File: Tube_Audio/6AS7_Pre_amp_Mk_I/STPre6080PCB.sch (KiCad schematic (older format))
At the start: 50 parts, among them J101 Screw_Terminal_01x02, J102 Screw_Terminal_01x04, J103 Screw_Terminal_01x03, J203 Screw_Terminal_01x03, Q101 ZVN0545A, Q102 ZVN0545A, Q201 ZVN0545A, Q202 ZVN0545A

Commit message: Checkpoint -- getting closer to laying out the tone control PCB.
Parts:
- C101, C201: footprint (none) -> jrt-Capacitors:C_Rect_L13.0mm_W5.0mm_P7.50mm
- C102, C106, C202, C206: footprint (none) -> Capacitor_THT:C_Rect_L18.0mm_W8.0mm_P15.00mm_FKS3_FKP3
- C103, C203: footprint (none) -> jrt-Capacitors:C_Rect_L18.0mm_W9.0mm_P8.70mm
- C104, C105, C204, C205: footprint (none) -> jrt-Capacitors:C_Rect_L13.0mm_W6.0mm_P5.90mm
- J101: footprint (none) -> TerminalBlock:TerminalBlock_bornier-2_P5.08mm
- J102: footprint (none) -> TerminalBlock:TerminalBlock_bornier-4_P5.08mm
- J103, J203: footprint (none) -> TerminalBlock:TerminalBlock_bornier-3_P5.08mm
- Q101, Q102, Q201, Q202: footprint (none) -> Package_TO_SOT_THT:TO-92_HandSolder
- R101, R201: footprint (none) -> Resistor_THT:R_Axial_DIN0414_L11.9mm_D4.5mm_P15.24mm_Horizontal; Part (none) -> KOA Speer MF1/2DC4703F
- R102, R202, R203: footprint (none) -> Resistor_THT:R_Axial_DIN0414_L11.9mm_D4.5mm_P15.24mm_Horizontal; Part (none) -> Vishay HVR3700001005FR500
- R103: footprint (none) -> Resistor_THT:R_Axial_DIN0414_L11.9mm_D4.5mm_P15.24mm_Horizontal; Part (none) -> HVR3700001005FR500
- R104, R112, R204, R212: footprint (none) -> Resistor_THT:R_Axial_DIN0414_L11.9mm_D4.5mm_P15.24mm_Horizontal
- R105, R113, R205, R213: value 56K -> 47K; footprint (none) -> Resistor_THT:R_Axial_DIN0414_L11.9mm_D4.5mm_P15.24mm_Horizontal; Part (none) -> TE H4P47KFZA
- R106, R107, R108, R109, R206, R207, R208, R209: footprint (none) -> Resistor_THT:R_Axial_DIN0207_L6.3mm_D2.5mm_P10.16mm_Horizontal; Part (none) -> TE H856KBDA
- R110, R210: footprint (none) -> Resistor_THT:R_Axial_DIN0207_L6.3mm_D2.5mm_P10.16mm_Horizontal; Part (none) -> TE H8470KBZA
- R111, R211: value 220K -> 221K; footprint (none) -> Resistor_THT:R_Axial_DIN0207_L6.3mm_D2.5mm_P10.16mm_Horizontal; Part (none) -> TE YR1B221KCC
- RV101, RV102, RV201, RV202: footprint (none) -> Connector_PinHeader_2.54mm:PinHeader_1x03_P2.54mm_Vertical
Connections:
- net +300V is gone; now on net +250V: Q101.3 (D), Q102.3 (D), Q201.3 (D), Q202.3 (D), R102.1, R202.1
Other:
- note added: "Baxandall network resistors are 0.1% 1/4W film resistors and 1% silvered mica capacitors.\nAll other resistors are 1% 1/2W film resistors unless otherwise indicated.\n\nTone control potentiometers are linear taper and panel mounted, not\nmounted on-board."
- note removed: "Baxandall network resistors are 0.1% 1/4W film resistors.\nAll other resistors are 1% 1/2W film resistors unless otherwise\nindicated.\n\nTone control potentiometers are linear taper and panel mounted, not\nmounted on-board."

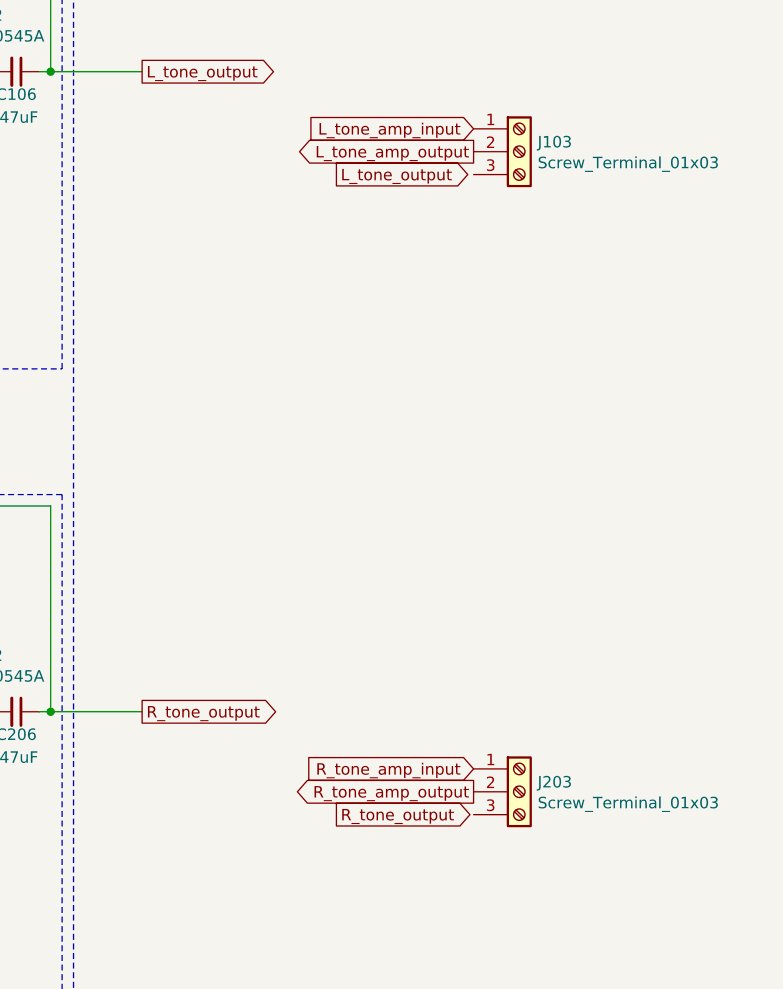
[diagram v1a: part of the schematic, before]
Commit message: A couple of small tweaks for laying out the PCB.
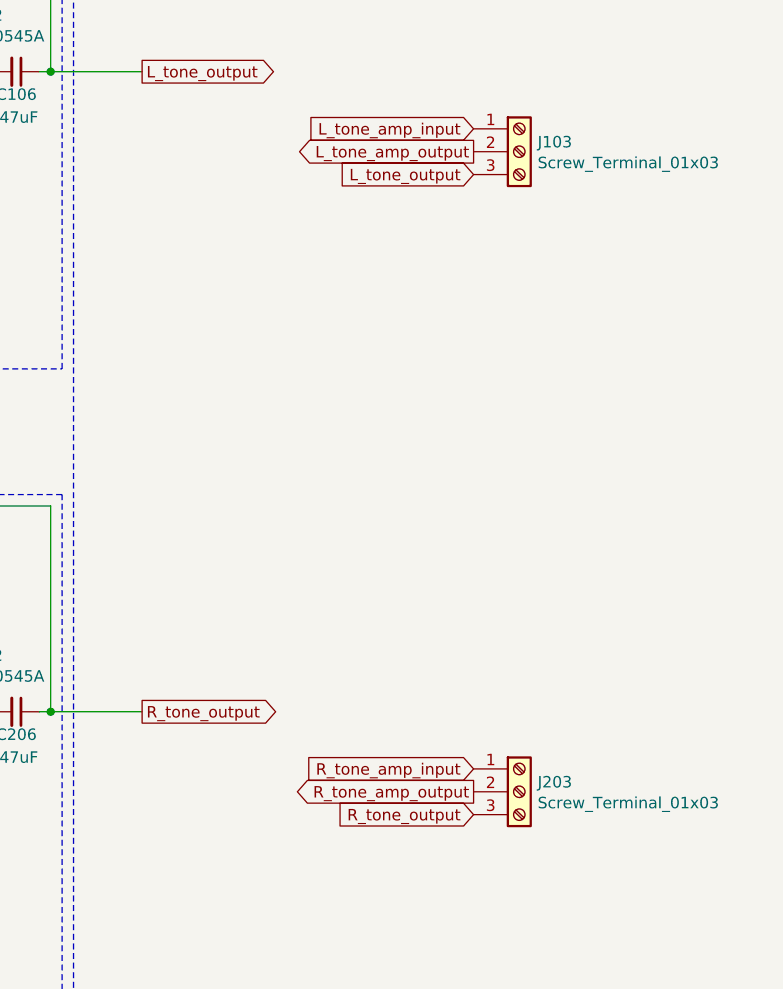
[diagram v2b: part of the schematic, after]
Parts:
- Q101, Q102, Q201, Q202: footprint Package_TO_SOT_THT:TO-92_HandSolder -> Package_TO_SOT_THT:TO-92_Wide
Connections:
- net L_tone_output: now also J103.3 (Pin_3)
- net R_tone_output: now also J203.3 (Pin_3)
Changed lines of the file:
@@
 F 0 "Q101" H 2556 1946 50  0000 L CNN
 F 1 "ZVN0545A" H 2556 1855 50  0000 L CNN
-F 2 "Package_TO_SOT_THT:TO-92_HandSolder" H 2550 2000 50  0001 C CNN
+F 2 "Package_TO_SOT_THT:TO-92_Wide" H 2550 2000 50  0001 C CNN
 F 3 "~" H 2350 1900 50  0001 C CNN
 	1    2350 1900
@@
 F 0 "Q102" H 7056 1596 50  0000 L CNN
 F 1 "ZVN0545A" H 7056 1505 50  0000 L CNN
-F 2 "Package_TO_SOT_THT:TO-92_HandSolder" H 7050 1650 50  0001 C CNN
+F 2 "Package_TO_SOT_THT:TO-92_Wide" H 7050 1650 50  0001 C CNN
 F 3 "~" H 6850 1550 50  0001 C CNN
 	1    6850 1550
@@
 F 0 "Q201" H 2556 4746 50  0000 L CNN
 F 1 "ZVN0545A" H 2556 4655 50  0000 L CNN
-F 2 "Package_TO_SOT_THT:TO-92_HandSolder" H 2550 4800 50  0001 C CNN
+F 2 "Package_TO_SOT_THT:TO-92_Wide" H 2550 4800 50  0001 C CNN
 F 3 "~" H 2350 4700 50  0001 C CNN
 	1    2350 4700
@@
 F 0 "Q202" H 7056 4396 50  0000 L CNN
 F 1 "ZVN0545A" H 7056 4305 50  0000 L CNN
-F 2 "Package_TO_SOT_THT:TO-92_HandSolder" H 7050 4450 50  0001 C CNN
+F 2 "Package_TO_SOT_THT:TO-92_Wide" H 7050 4450 50  0001 C CNN
 F 3 "~" H 6850 4350 50  0001 C CNN
 	1    6850 4350
@@
 Text GLabel 9300 2100 0    50   Output ~ 0
 L_tone_amp_output
-Text GLabel 8700 2200 2    50   Output ~ 0
+Text GLabel 9300 2200 0    50   Input ~ 0
 L_tone_output
 Text GLabel 9300 4800 0    50   Input ~ 0
@@
 Text GLabel 9300 4900 0    50   Output ~ 0
 R_tone_amp_output
-Text GLabel 8700 5000 2    50   Output ~ 0
+Text GLabel 9300 5000 0    50   Input ~ 0
 R_tone_output
 $Comp
